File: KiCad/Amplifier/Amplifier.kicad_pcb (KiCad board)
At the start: 2 copper layers, 1 part

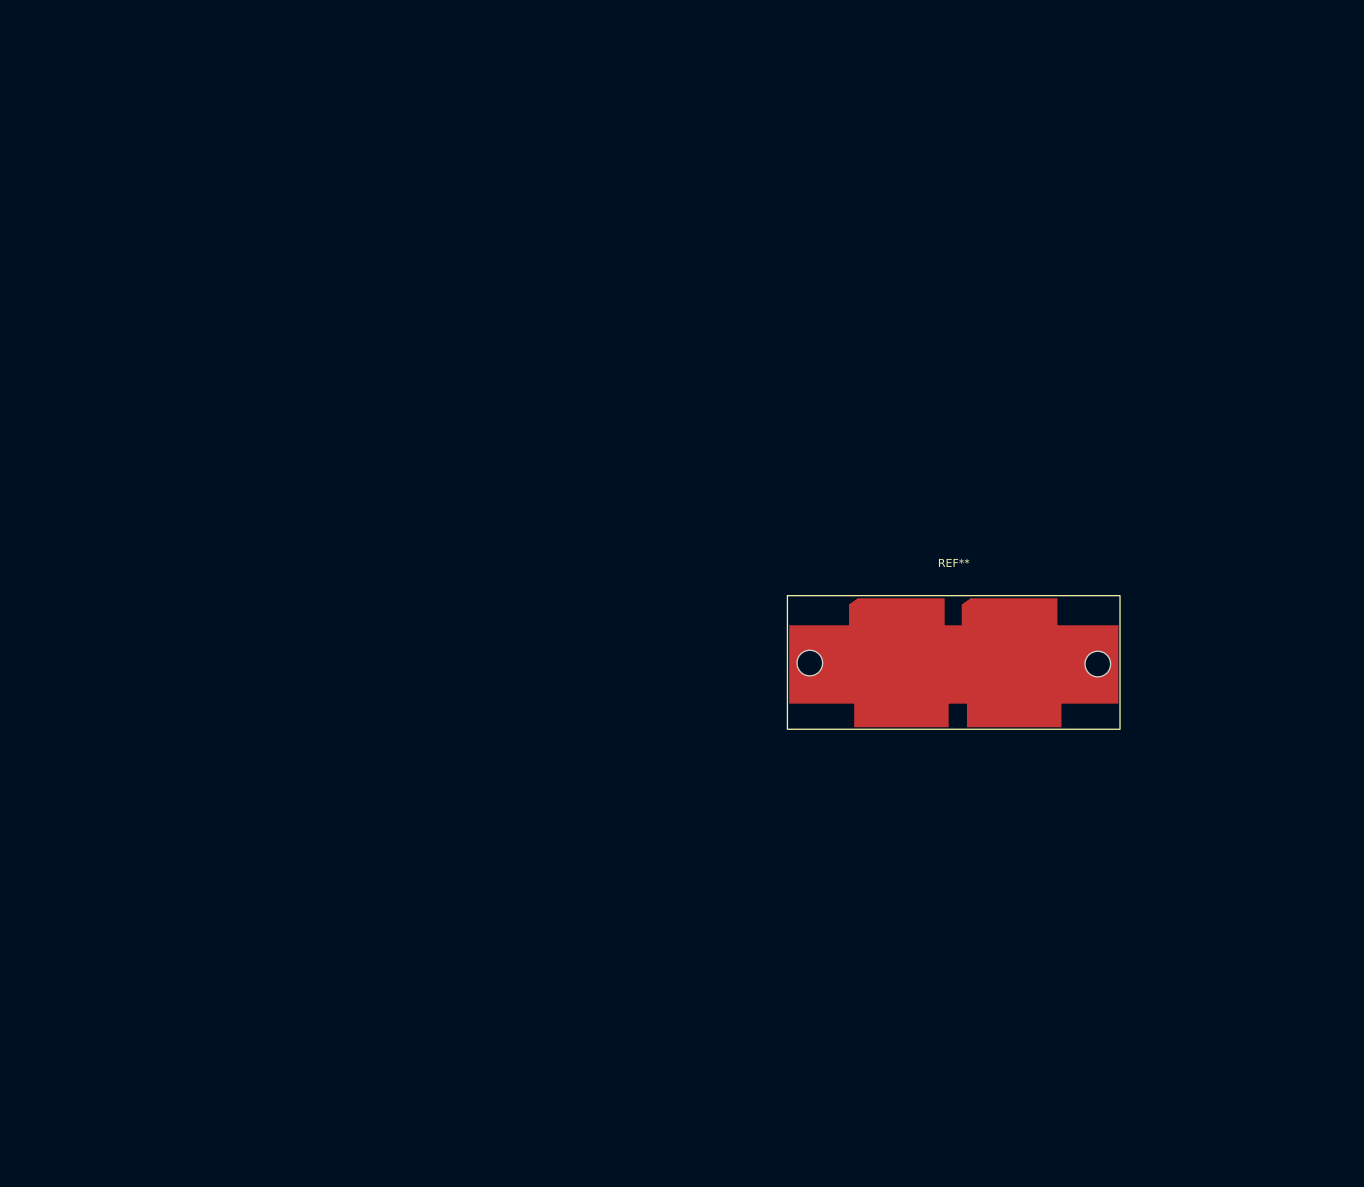
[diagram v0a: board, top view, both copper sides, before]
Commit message: Platinenentwurf
die Platine wurde aufgebaut. Kontrolle fehlt
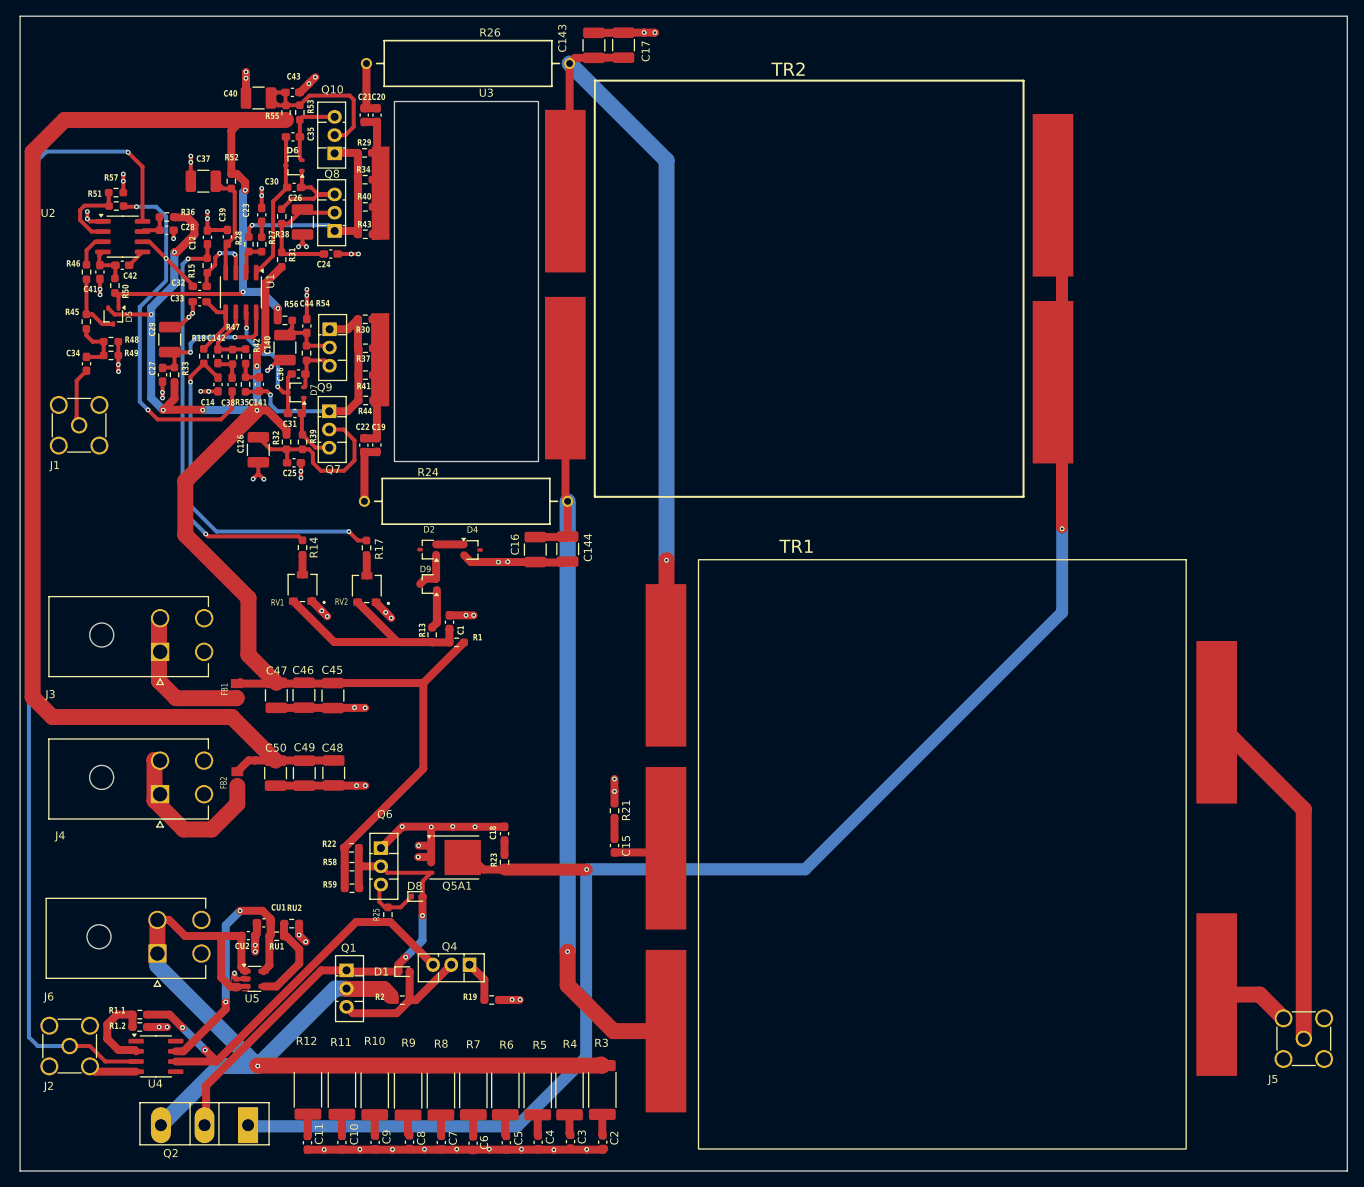
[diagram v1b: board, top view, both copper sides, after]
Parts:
- removed REF**: SOT539A, Library:SOT539A
- added C1: 0.1uF, Capacitor_SMD:C_0603_1608Metric_Pad1.08x0.95mm_HandSolder, F.Cu at (84.0, 92.9)
- added C10: 0.1uF, Capacitor_SMD:C_0603_1608Metric_Pad1.08x0.95mm_HandSolder, F.Cu at (70.5, 157.9)
- added C11: 0.1uF, Capacitor_SMD:C_0603_1608Metric_Pad1.08x0.95mm_HandSolder, F.Cu at (66.2, 157.9)
- added C12: 0.1uF, Capacitor_SMD:C_0603_1608Metric_Pad1.08x0.95mm_HandSolder, F.Cu at (53.7, 44.8)
- added C126: 10uF, Capacitor_SMD:C_1210_3225Metric_Pad1.33x2.70mm_HandSolder, F.Cu at (60.1, 71.3)
- added C14: 0.1uF, Capacitor_SMD:C_0603_1608Metric_Pad1.08x0.95mm_HandSolder, F.Cu at (55.0, 63.2)
- added C140: 10uF, Capacitor_SMD:C_1210_3225Metric_Pad1.33x2.70mm_HandSolder, F.Cu at (63.4, 58.5)
- added C141: 10p, Capacitor_SMD:C_0603_1608Metric_Pad1.08x0.95mm_HandSolder, F.Cu at (60.2, 63.1)
- added C142: NDA, Capacitor_SMD:C_0603_1608Metric_Pad1.08x0.95mm_HandSolder, F.Cu at (55.0, 59.6)
- added C143: 470p, Capacitor_SMD:C_1210_3225Metric_Pad1.33x2.70mm_HandSolder, F.Cu at (102.0, 20.8)
- added C144: 470p, Capacitor_SMD:C_1210_3225Metric_Pad1.33x2.70mm_HandSolder, F.Cu at (98.7, 83.7)
- added C15: 0.1uF, Capacitor_SMD:C_0603_1608Metric_Pad1.08x0.95mm_HandSolder, F.Cu at (104.6, 120.8)
- added C16: 470p, Capacitor_SMD:C_1210_3225Metric_Pad1.33x2.70mm_HandSolder, F.Cu at (94.7, 83.8)
- added C17: 470p, Capacitor_SMD:C_1210_3225Metric_Pad1.33x2.70mm_HandSolder, F.Cu at (105.7, 20.7)
- added C18: 1nF, Capacitor_SMD:C_0603_1608Metric_Pad1.08x0.95mm_HandSolder, F.Cu at (90.8, 119.3)
- added C19: 1nF, Capacitor_SMD:C_0603_1608Metric_Pad1.08x0.95mm_HandSolder, F.Cu at (74.9, 70.7)
- added C2: 0.1uF, Capacitor_SMD:C_0603_1608Metric_Pad1.08x0.95mm_HandSolder, F.Cu at (103.1, 157.9)
- added C20: 1nF, Capacitor_SMD:C_0603_1608Metric_Pad1.08x0.95mm_HandSolder, F.Cu at (74.9, 29.5)
- added C21: DNA, Capacitor_SMD:C_0603_1608Metric_Pad1.08x0.95mm_HandSolder, F.Cu at (73.3, 29.5)
- added C22: DNA, Capacitor_SMD:C_0603_1608Metric_Pad1.08x0.95mm_HandSolder, F.Cu at (73.3, 70.7)
- added C23: 0.1uF, Capacitor_SMD:C_0603_1608Metric_Pad1.08x0.95mm_HandSolder, F.Cu at (60.5, 41.9)
- added C24: 0.1uF, Capacitor_SMD:C_0603_1608Metric_Pad1.08x0.95mm_HandSolder, F.Cu at (69.1, 46.8)
- added C25: 0.1uF, Capacitor_SMD:C_0603_1608Metric_Pad1.08x0.95mm_HandSolder, F.Cu at (64.5, 72.9)
- added C26: 10uF, Capacitor_SMD:C_1210_3225Metric_Pad1.33x2.70mm_HandSolder, F.Cu at (65.6, 42.8)
- added C27: 0.1uF, Capacitor_SMD:C_0603_1608Metric_Pad1.08x0.95mm_HandSolder, F.Cu at (48.1, 61.9)
- added C28: 0.1uF, Capacitor_SMD:C_0603_1608Metric_Pad1.08x0.95mm_HandSolder, F.Cu at (48.6, 43.9)
- added C29: 10uF, Capacitor_SMD:C_1210_3225Metric_Pad1.33x2.70mm_HandSolder, F.Cu at (49.0, 57.5)
- added C3: 0.1uF, Capacitor_SMD:C_0603_1608Metric_Pad1.08x0.95mm_HandSolder, F.Cu at (99.1, 157.8)
- added C30: 0.1uF, Capacitor_SMD:C_0603_1608Metric_Pad1.08x0.95mm_HandSolder, F.Cu at (64.5, 38.5)
- added C31: 0.1uF, Capacitor_SMD:C_0603_1608Metric_Pad1.08x0.95mm_HandSolder, F.Cu at (64.6, 66.8)
- added C32: 0.1uF, Capacitor_SMD:C_0603_1608Metric_Pad1.08x0.95mm_HandSolder, F.Cu at (52.7, 50.9)
- added C33: 0.1uF, Capacitor_SMD:C_0603_1608Metric_Pad1.08x0.95mm_HandSolder, F.Cu at (52.7, 52.8)
- added C34: 4n7, Capacitor_SMD:C_0603_1608Metric_Pad1.08x0.95mm_HandSolder, F.Cu at (38.6, 60.6)
- added C35: 0.1uF, Capacitor_SMD:C_0603_1608Metric_Pad1.08x0.95mm_HandSolder, F.Cu at (64.4, 32.2)
- added C36: 0.1uF, Capacitor_SMD:C_0603_1608Metric_Pad1.08x0.95mm_HandSolder, F.Cu at (65.1, 61.8)
- added C37: 10uF, Capacitor_SMD:C_1210_3225Metric_Pad1.33x2.70mm_HandSolder, F.Cu at (53.2, 37.7)
- added C38: 0.1uF, Capacitor_SMD:C_0603_1608Metric_Pad1.08x0.95mm_HandSolder, F.Cu at (56.8, 63.2)
- added C39: 0.1uF, Capacitor_SMD:C_0603_1608Metric_Pad1.08x0.95mm_HandSolder, F.Cu at (56.2, 44.7)
- added C4: 0.1uF, Capacitor_SMD:C_0603_1608Metric_Pad1.08x0.95mm_HandSolder, F.Cu at (95.0, 157.9)
- added C40: 10uF, Capacitor_SMD:C_1210_3225Metric_Pad1.33x2.70mm_HandSolder, F.Cu at (60.1, 27.3)
- added C41: 0.1uF, Capacitor_SMD:C_0603_1608Metric_Pad1.08x0.95mm_HandSolder, F.Cu at (40.3, 49.1)
- added C42: 10p, Capacitor_SMD:C_0603_1608Metric_Pad1.08x0.95mm_HandSolder, F.Cu at (43.1, 48.2)
- added C43: 0.1uF, Capacitor_SMD:C_0603_1608Metric_Pad1.08x0.95mm_HandSolder, F.Cu at (64.3, 26.6)
- added C44: 0.1uF, Capacitor_SMD:C_0603_1608Metric_Pad1.08x0.95mm_HandSolder, F.Cu at (66.1, 55.8)
- added C45: 10uF, Capacitor_SMD:C_1210_3225Metric_Pad1.33x2.70mm_HandSolder, F.Cu at (69.4, 102.0)
- added C46: 10uF, Capacitor_SMD:C_1210_3225Metric_Pad1.33x2.70mm_HandSolder, F.Cu at (65.8, 102.0)
- added C47: 10uF, Capacitor_SMD:C_1210_3225Metric_Pad1.33x2.70mm_HandSolder, F.Cu at (62.3, 102.0)
- added C48: 10uF, Capacitor_SMD:C_1210_3225Metric_Pad1.33x2.70mm_HandSolder, F.Cu at (69.5, 111.7)
- added C49: 10uF, Capacitor_SMD:C_1210_3225Metric_Pad1.33x2.70mm_HandSolder, F.Cu at (65.8, 111.7)
- added C5: 0.1uF, Capacitor_SMD:C_0603_1608Metric_Pad1.08x0.95mm_HandSolder, F.Cu at (91.1, 157.9)
- added C50: 10uF, Capacitor_SMD:C_1210_3225Metric_Pad1.33x2.70mm_HandSolder, F.Cu at (62.2, 111.7)
- added C6: 0.1uF, Capacitor_SMD:C_0603_1608Metric_Pad1.08x0.95mm_HandSolder, F.Cu at (86.9, 158.0)
- added C7: 0.1uF, Capacitor_SMD:C_0603_1608Metric_Pad1.08x0.95mm_HandSolder, F.Cu at (82.9, 157.9)
- added C8: 0.1uF, Capacitor_SMD:C_0603_1608Metric_Pad1.08x0.95mm_HandSolder, F.Cu at (79.0, 157.9)
- added C9: 0.1uF, Capacitor_SMD:C_0603_1608Metric_Pad1.08x0.95mm_HandSolder, F.Cu at (74.7, 157.9)
- added CU1: 1uF, Capacitor_SMD:C_0603_1608Metric_Pad1.08x0.95mm_HandSolder, F.Cu at (60.8, 130.4)
- added CU2: 1uF, Capacitor_SMD:C_0603_1608Metric_Pad1.08x0.95mm_HandSolder, F.Cu at (58.8, 132.1)
- added D1: BAT54XV2T5G, Library:D_SOD-523_new, F.Cu at (78.3, 136.5)
- added D2: BAV99WT1G, Package_TO_SOT_SMD:SOT-323_SC-70, F.Cu at (81.3, 83.8)
- added D4: BAV99WT1G, Package_TO_SOT_SMD:SOT-323_SC-70, F.Cu at (86.8, 83.8)
- added D5: BAV99WT1G, Package_TO_SOT_SMD:SOT-323_SC-70, F.Cu at (41.9, 54.6)
- added D6: BAV99WT1G, Package_TO_SOT_SMD:SOT-323_SC-70, F.Cu at (64.5, 35.8)
- added D7: BAV99WT1G, Package_TO_SOT_SMD:SOT-323_SC-70, F.Cu at (64.8, 64.2)
- added D8: BAT54XV2T5G, Library:D_SOD-523_new, F.Cu at (79.9, 127.2)
- added D9: BAV99WT1G, Package_TO_SOT_SMD:SOT-323_SC-70, F.Cu at (81.3, 88.1)
- added FB1: FerriteBead, Library:BLM21PG300SN1B, F.Cu at (57.4, 101.4)
- added FB2: FerriteBead, Library:BLM21PG300SN1B, F.Cu at (57.4, 112.4)
- added J1: Input, Connector_Coaxial:SMA_Amphenol_901-144_Vertical, F.Cu at (37.7, 68.2)
- added J2: Enable, Connector_Coaxial:SMA_Amphenol_901-144_Vertical, F.Cu at (36.5, 145.8)
- added J3: Vp_8V, Library:MOLEX_26013115, F.Cu at (47.8, 96.6)
- added J4: Vn_-5V, Library:MOLEX_26013115, F.Cu at (47.8, 114.4)
- added J5: Output, Connector_Coaxial:SMA_Amphenol_901-144_Vertical, F.Cu at (190.7, 144.9)
- added J6: Input_56V, Library:MOLEX_26013115, F.Cu at (47.5, 134.3)
- added Q1: BD139, Package_TO_SOT_THT:TO-126-3_Vertical, F.Cu at (71.1, 136.4)
- added Q10: BD140, Package_TO_SOT_THT:TO-126-3_Vertical, F.Cu at (69.6, 34.3)
- added Q2: IXTH90P10P, Library:TO-247-3_MOSFET, F.Cu at (58.8, 155.7)
- added Q4: BD139, Package_TO_SOT_THT:TO-126-3_Vertical, F.Cu at (86.5, 135.7)
- added Q5A1: BSC340N08NS3G, Package_TO_SOT_SMD:TDSON-8-1, F.Cu at (84.6, 122.3)
- added Q6: BD139, Package_TO_SOT_THT:TO-126-3_Vertical, F.Cu at (75.4, 121.1)
- added Q7: BD139, Package_TO_SOT_THT:TO-126-3_Vertical, F.Cu at (68.9, 66.5)
- added Q8: BD139, Package_TO_SOT_THT:TO-126-3_Vertical, F.Cu at (69.6, 44.0)
- added Q9: BD140, Package_TO_SOT_THT:TO-126-3_Vertical, F.Cu at (69.0, 56.3)
- added R1: 4k7, Resistor_SMD:R_0603_1608Metric_Pad0.98x0.95mm_HandSolder, F.Cu at (84.9, 95.4)
- added R1.1: 10k, Resistor_SMD:R_0603_1608Metric_Pad0.98x0.95mm_HandSolder, F.Cu at (45.2, 141.9)
- added R1.2: 2k, Resistor_SMD:R_0603_1608Metric_Pad0.98x0.95mm_HandSolder, F.Cu at (45.2, 143.5)
- added R10: 2R2, Resistor_SMD:R_2512_6332Metric_Pad1.40x3.35mm_HandSolder, F.Cu at (74.6, 151.4)
- added R11: 2R2, Resistor_SMD:R_2512_6332Metric_Pad1.40x3.35mm_HandSolder, F.Cu at (70.5, 151.3)
- added R12: 2R2, Resistor_SMD:R_2512_6332Metric_Pad1.40x3.35mm_HandSolder, F.Cu at (66.3, 151.3)
- added R13: 120R, Resistor_SMD:R_0603_1608Metric_Pad0.98x0.95mm_HandSolder, F.Cu at (81.8, 94.4)
- added R14: 120R, Resistor_SMD:R_0603_1608Metric_Pad0.98x0.95mm_HandSolder, F.Cu at (65.6, 83.5)
- added R15: 4k7, Resistor_SMD:R_0603_1608Metric_Pad0.98x0.95mm_HandSolder, F.Cu at (53.7, 48.3)
- added R17: 120R, Resistor_SMD:R_0603_1608Metric_Pad0.98x0.95mm_HandSolder, F.Cu at (73.6, 83.6)
- added R18: 4k7, Resistor_SMD:R_0603_1608Metric_Pad0.98x0.95mm_HandSolder, F.Cu at (53.2, 59.6)
- added R19: 120R, Resistor_SMD:R_0603_1608Metric_Pad0.98x0.95mm_HandSolder, F.Cu at (89.2, 140.1)
- added R2: 330R, Resistor_SMD:R_0603_1608Metric_Pad0.98x0.95mm_HandSolder, F.Cu at (78.1, 140.1)
- added R21: 22R, Resistor_SMD:R_0603_1608Metric_Pad0.98x0.95mm_HandSolder, F.Cu at (104.6, 116.4)
- added R22: 220R, Resistor_SMD:R_0603_1608Metric_Pad0.98x0.95mm_HandSolder, F.Cu at (71.7, 121.1)
- added R23: 2R2, Resistor_SMD:R_0603_1608Metric_Pad0.98x0.95mm_HandSolder, F.Cu at (90.8, 122.9)
- added R24: 270R, Library:AX_1.000X.225_.034, F.Cu at (88.1, 78.2)
- added R25: 4k7, Resistor_SMD:R_0603_1608Metric_Pad0.98x0.95mm_HandSolder, F.Cu at (76.3, 129.4)
- added R26: 270R, Library:AX_1.000X.225_.034, F.Cu at (88.4, 23.5)
- added R27: 470R, Resistor_SMD:R_0603_1608Metric_Pad0.98x0.95mm_HandSolder, F.Cu at (60.5, 45.6)
- added R28: 470R, Resistor_SMD:R_0603_1608Metric_Pad0.98x0.95mm_HandSolder, F.Cu at (58.9, 45.6)
- added R29: 39R, Resistor_SMD:R_0603_1608Metric_Pad0.98x0.95mm_HandSolder, F.Cu at (73.4, 34.2)
- added R3: 2R2, Resistor_SMD:R_2512_6332Metric_Pad1.40x3.35mm_HandSolder, F.Cu at (103.1, 151.3)
- added R30: 39R, Resistor_SMD:R_0603_1608Metric_Pad0.98x0.95mm_HandSolder, F.Cu at (73.4, 55.0)
- added R31: 2R2, Resistor_SMD:R_0603_1608Metric_Pad0.98x0.95mm_HandSolder, F.Cu at (63.0, 47.5)
- added R32: 2R2, Resistor_SMD:R_0603_1608Metric_Pad0.98x0.95mm_HandSolder, F.Cu at (63.6, 70.3)
- added R33: 2R2, Resistor_SMD:R_0603_1608Metric_Pad0.98x0.95mm_HandSolder, F.Cu at (49.6, 61.9)
- added R34: 39R, Resistor_SMD:R_0603_1608Metric_Pad0.98x0.95mm_HandSolder, F.Cu at (73.4, 37.6)
- added R35: 220R, Resistor_SMD:R_0603_1608Metric_Pad0.98x0.95mm_HandSolder, F.Cu at (58.5, 63.2)
- added R36: 2R2, Resistor_SMD:R_0603_1608Metric_Pad0.98x0.95mm_HandSolder, F.Cu at (48.6, 42.2)
- added R37: 39R, Resistor_SMD:R_0603_1608Metric_Pad0.98x0.95mm_HandSolder, F.Cu at (73.5, 58.6)
- added R38: 10k, Resistor_SMD:R_0603_1608Metric_Pad0.98x0.95mm_HandSolder, F.Cu at (63.0, 42.1)
- added R39: 10k, Resistor_SMD:R_0603_1608Metric_Pad0.98x0.95mm_HandSolder, F.Cu at (65.6, 70.3)
- added R4: 2R2, Resistor_SMD:R_2512_6332Metric_Pad1.40x3.35mm_HandSolder, F.Cu at (99.0, 151.4)
- added R40: 39R, Resistor_SMD:R_0603_1608Metric_Pad0.98x0.95mm_HandSolder, F.Cu at (73.4, 41.0)
- added R41: 39R, Resistor_SMD:R_0603_1608Metric_Pad0.98x0.95mm_HandSolder, F.Cu at (73.5, 62.0)
- added R42: 220R, Resistor_SMD:R_0603_1608Metric_Pad0.98x0.95mm_HandSolder, F.Cu at (58.5, 59.6)
- added R43: 39R, Resistor_SMD:R_0603_1608Metric_Pad0.98x0.95mm_HandSolder, F.Cu at (73.4, 44.4)
- added R44: 39R, Resistor_SMD:R_0603_1608Metric_Pad0.98x0.95mm_HandSolder, F.Cu at (73.5, 65.2)
- added R45: 100R, Resistor_SMD:R_0603_1608Metric_Pad0.98x0.95mm_HandSolder, F.Cu at (38.6, 55.3)
- added R46: 100R, Resistor_SMD:R_0603_1608Metric_Pad0.98x0.95mm_HandSolder, F.Cu at (38.6, 49.1)
- added R47: 220R, Resistor_SMD:R_0603_1608Metric_Pad0.98x0.95mm_HandSolder, F.Cu at (56.8, 59.7)
- added R48: 100R, Resistor_SMD:R_0603_1608Metric_Pad0.98x0.95mm_HandSolder, F.Cu at (41.6, 57.8)
- added R49: 100R, Resistor_SMD:R_0603_1608Metric_Pad0.98x0.95mm_HandSolder, F.Cu at (41.6, 59.5)
- added R5: 2R2, Resistor_SMD:R_2512_6332Metric_Pad1.40x3.35mm_HandSolder, F.Cu at (95.0, 151.4)
- added R50: 2R2, Resistor_SMD:R_0603_1608Metric_Pad0.98x0.95mm_HandSolder, F.Cu at (42.1, 50.8)
- added R51: 470R, Resistor_SMD:R_0603_1608Metric_Pad0.98x0.95mm_HandSolder, F.Cu at (42.3, 40.8)
- added R52: 2R2, Resistor_SMD:R_0603_1608Metric_Pad0.98x0.95mm_HandSolder, F.Cu at (56.7, 37.7)
- added R53: 10k, Resistor_SMD:R_0603_1608Metric_Pad0.98x0.95mm_HandSolder, F.Cu at (65.3, 29.2)
- added R54: 10k, Resistor_SMD:R_0603_1608Metric_Pad0.98x0.95mm_HandSolder, F.Cu at (66.1, 59.2)
- added R55: 2R2, Resistor_SMD:R_0603_1608Metric_Pad0.98x0.95mm_HandSolder, F.Cu at (63.5, 29.2)
- added R56: 2R2, Resistor_SMD:R_0603_1608Metric_Pad0.98x0.95mm_HandSolder, F.Cu at (63.4, 55.1)
- added R57: 470R, Resistor_SMD:R_0603_1608Metric_Pad0.98x0.95mm_HandSolder, F.Cu at (42.3, 39.2)
- added R58: 220R, Resistor_SMD:R_0603_1608Metric_Pad0.98x0.95mm_HandSolder, F.Cu at (71.8, 123.4)
- added R59: 220R, Resistor_SMD:R_0603_1608Metric_Pad0.98x0.95mm_HandSolder, F.Cu at (71.8, 126.1)
- added R6: 2R2, Resistor_SMD:R_2512_6332Metric_Pad1.40x3.35mm_HandSolder, F.Cu at (90.9, 151.4)
- added R7: 2R2, Resistor_SMD:R_2512_6332Metric_Pad1.40x3.35mm_HandSolder, F.Cu at (86.9, 151.4)
- added R8: 2R2, Resistor_SMD:R_2512_6332Metric_Pad1.40x3.35mm_HandSolder, F.Cu at (82.9, 151.4)
- added R9: 2R2, Resistor_SMD:R_2512_6332Metric_Pad1.40x3.35mm_HandSolder, F.Cu at (78.8, 151.4)
- added RU1: 25.2k, Resistor_SMD:R_0603_1608Metric_Pad0.98x0.95mm_HandSolder, F.Cu at (62.4, 132.1)
- added RU2: 1.35k, Resistor_SMD:R_0603_1608Metric_Pad0.98x0.95mm_HandSolder, F.Cu at (64.2, 130.5)
- added RV1: R_Potentiometer, Library:PVG3A, F.Cu at (65.6, 88.6)
- added RV2: R_Potentiometer, Library:PVG3A, F.Cu at (73.6, 88.7)
- added TR1: 1:1:4:4, Library:TR1, F.Cu at (143.0, 121.6)
- added TR2: 1:1, Library:TR2, F.Cu at (140.6, 81.7)
- added U1: AD8017ARZ, Package_SO:SOIC-8_3.9x4.9mm_P1.27mm, F.Cu at (57.9, 51.6)
- added U2: AD8021AR, Package_SO:SOIC-8_3.9x4.9mm_P1.27mm, F.Cu at (43.1, 44.7)
- added U3: BLF188XRU, Library:SOT539A, F.Cu at (86.1, 36.4)
- added U4: AD8033, Package_SO:SOIC-8_3.9x4.9mm_P1.27mm, F.Cu at (47.3, 147.1)
- added U5: LT3014xS5, Package_TO_SOT_SMD:SOT-23-5, F.Cu at (59.6, 137.4)
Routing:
- net Output_56V: track 0.00 -> 209.9 mm, vias 0 -> 2
- net Vn: track 0.00 -> 201.5 mm, vias 0 -> 3
- net GND: track 0.00 -> 198.2 mm, vias 0 -> 77
- net Vp: track 0.00 -> 177.7 mm, vias 0 -> 6
- net Enable: track 0.00 -> 145.9 mm, vias 0 -> 1
- net Input_56V: track 0.00 -> 128.7 mm, vias 0 -> 1
- net /HF Part/D1: track 0.00 -> 103.7 mm, vias 0 -> 1
- net /HF Part/D2: track 0.00 -> 99.3 mm, vias 0 -> 1
- net /Switch/G: track 0.00 -> 63.3 mm, vias 0 -> 2
- net Output_OPV1: track 0.00 -> 54.2 mm, vias 0 -> 3
- net /Switch/ENA: track 0.00 -> 52.7 mm, vias 0 -> 2
- net Net-(C12-Pad1): track 0.00 -> 52.5 mm, vias 0 -> 2
- net Net-(C14-Pad1): track 0.00 -> 44.8 mm, vias 0 -> 2
- net /HF Part/Output: track 0.00 -> 44.1 mm
- net Net-(U4-V+): track 0.00 -> 32.6 mm, vias 0 -> 2
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- added copper zone on F.Cu, net GND
- added copper zone on In1.Cu, net GND
- added copper zone on F.Cu, net Input_56V
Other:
- board outline added: 165.9 x 144.3 mm
- copper layers 2 -> 4

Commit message: Update PCB
update PCB
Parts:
- added H1: MountingHole, MountingHole:MountingHole_3.2mm_M3_Pad, F.Cu at (34.6, 21.7)
- added H2: MountingHole, MountingHole:MountingHole_3.2mm_M3_Pad, F.Cu at (191.2, 21.8)
- added H3: MountingHole, MountingHole:MountingHole_3.2mm_M3_Pad, F.Cu at (34.6, 156.7)
- added H4: MountingHole, MountingHole:MountingHole_3.2mm_M3_Pad, F.Cu at (191.0, 156.9)
- moved C15 49.4 mm to (135.8, 82.4)
- moved R21 47.3 mm to (137.4, 82.4), turned to -90 degrees
- moved TR2 27.7 mm to (129.7, 56.2)
- moved TR1 2.88 mm to (142.1, 118.9), turned to 180 degrees
- moved J6 0.37 mm to (47.8, 134.1)
- moved J3 0.19 mm to (47.6, 96.5)
- moved J5 0.17 mm to (190.6, 144.9)
- moved J4 0.17 mm to (47.6, 114.3)
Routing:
- net Output_56V: track 209.9 -> 88.3 mm, vias 2 -> 10
- net /HF Part/D1: track 103.7 -> 23.4 mm, vias 1 -> 0
- net /HF Part/D2: track 99.3 -> 23.7 mm, vias 1 -> 0
- net GND: track 198.2 -> 188.1 mm, vias 77 -> 83
- net Net-(J4-Pin_1): track 20.5 -> 25.2 mm
- net /HF Part/Output: track 44.1 -> 39.9 mm
- net Vp: track 177.7 -> 180.0 mm
- net Net-(TR1-PM): track 6.70 -> 8.81 mm
- net Input_56V: track 128.7 -> 127.4 mm
- net Net-(C15-Pad1): track 2.58 -> 1.67 mm
- added copper zone on F.Cu, net /HF Part/D1
- added copper zone on F.Cu, net /HF Part/D2
- added copper zone on B.Cu, net Output_56V
- added copper zone on F.Cu, net Output_56V
